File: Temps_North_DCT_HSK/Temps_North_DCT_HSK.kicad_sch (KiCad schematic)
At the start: 4 parts, among them J1 North_Temps_1, J2 North_Temps_2, J3 Internal_Temps_DCT_HSK_Box_1, J4 Internal_Temps_DCT_HSK_Box_2

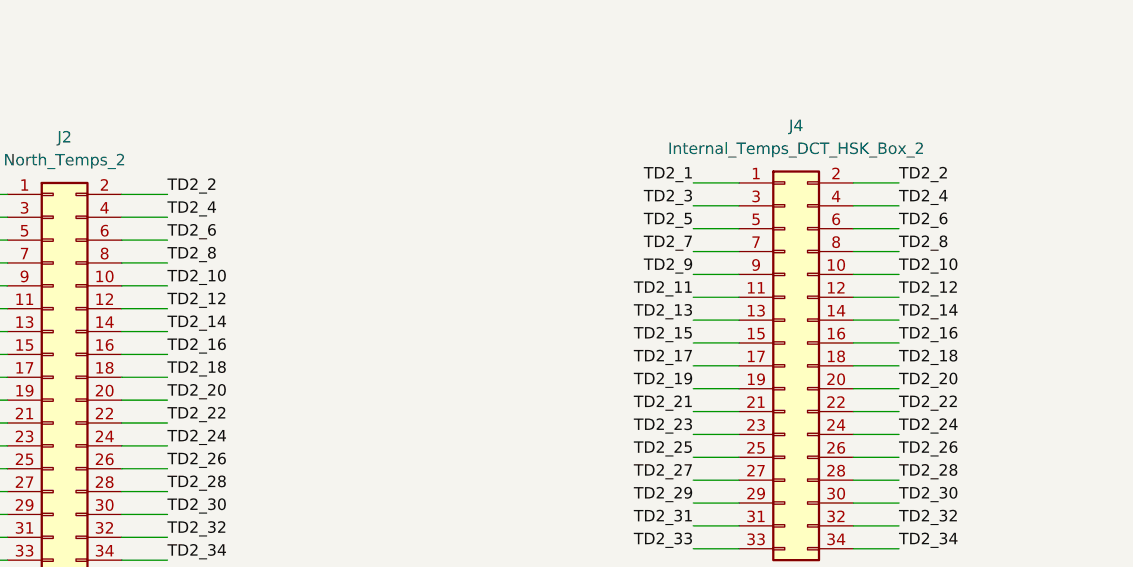
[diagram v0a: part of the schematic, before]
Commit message: Corrected pinout for from NTB2 to DCT HSK
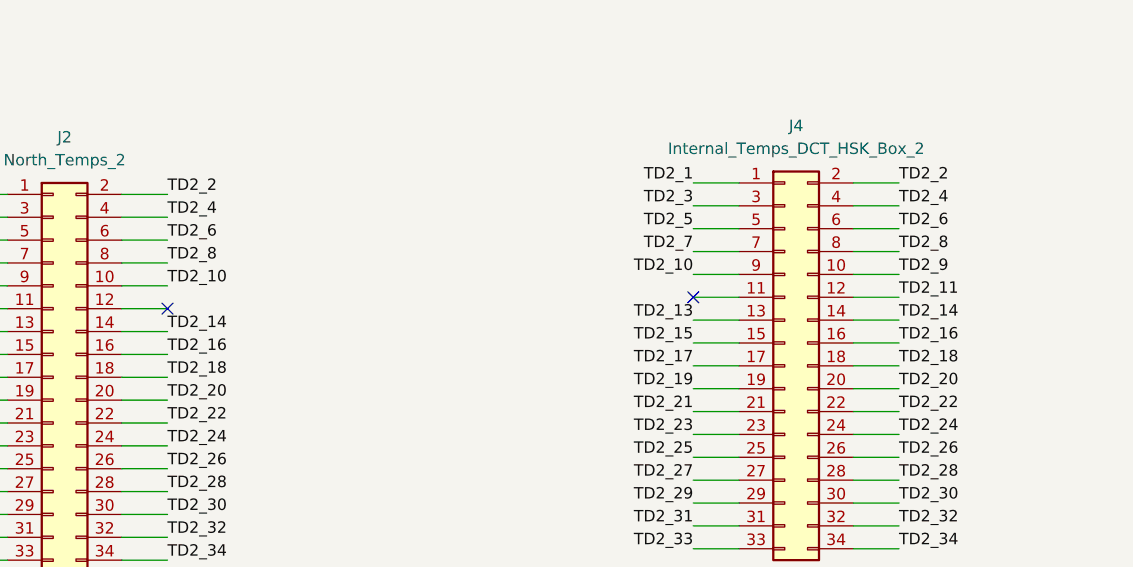
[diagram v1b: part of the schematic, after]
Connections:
- net TD2_10: now also J4.9 (Pin_9); no longer J4.10 (Pin_10)
- net TD2_11: now also J4.12 (Pin_12); no longer J4.11 (Pin_11)
- net TD2_9: now also J4.10 (Pin_10); no longer J4.9 (Pin_9)
- net TD2_12: no longer names the net of J2.12 (Pin_12)
- net TD2_12: no longer J4.12 (Pin_12)
- no-connect marks 0 -> 2
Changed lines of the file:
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@@
     (company "The Ohio State University")
   )
+  (no_connect (at 99.06 130.81))
+  (no_connect (at 157.48 129.54))
   (wire (pts (xy 160.02 78.74) (xy 165.1 78.74))
     (stroke (width 0) (type default) (color 0 0 0 0))
@@
     (effects (font (size 1.27 1.27)) (justify right bottom))
   )
-  (label "TD2_12" (at 180.34 129.54 0)
+  (label "TD2_11" (at 180.34 129.54 0)
     (effects (font (size 1.27 1.27)) (justify left bottom))
   )
@@
     (effects (font (size 1.27 1.27)) (justify right bottom))
   )
-  (label "TD2_11" (at 157.48 129.54 180)
-    (effects (font (size 1.27 1.27)) (justify right bottom))
-  )
   (label "TD1_4" (at 182.88 43.18 0)
     (effects (font (size 1.27 1.27)) (justify left bottom))
@@
     (effects (font (size 1.27 1.27)) (justify right bottom))
   )
-  (label "TD2_9" (at 157.48 127 180)
+  (label "TD2_10" (at 157.48 127 180)
     (effects (font (size 1.27 1.27)) (justify right bottom))
   )
@@
     (effects (font (size 1.27 1.27)) (justify left bottom))
   )
-  (label "TD2_12" (at 99.06 130.81 0)
-    (effects (font (size 1.27 1.27)) (justify left bottom))
-  )
   (label "TD2_2" (at 99.06 118.11 0)
     (effects (font (size 1.27 1.27)) (justify left bottom))
@@
     (effects (font (size 1.27 1.27)) (justify right bottom))
   )
-  (label "TD2_10" (at 180.34 127 0)
-    (effects (font (size 1.27 1.27)) (justify left bottom))
-  )
+  (label "TD2_9" (at 180.34 127 0)
+    (effects (font (size 1.27 1.27)) (justify left bottom))
+  )

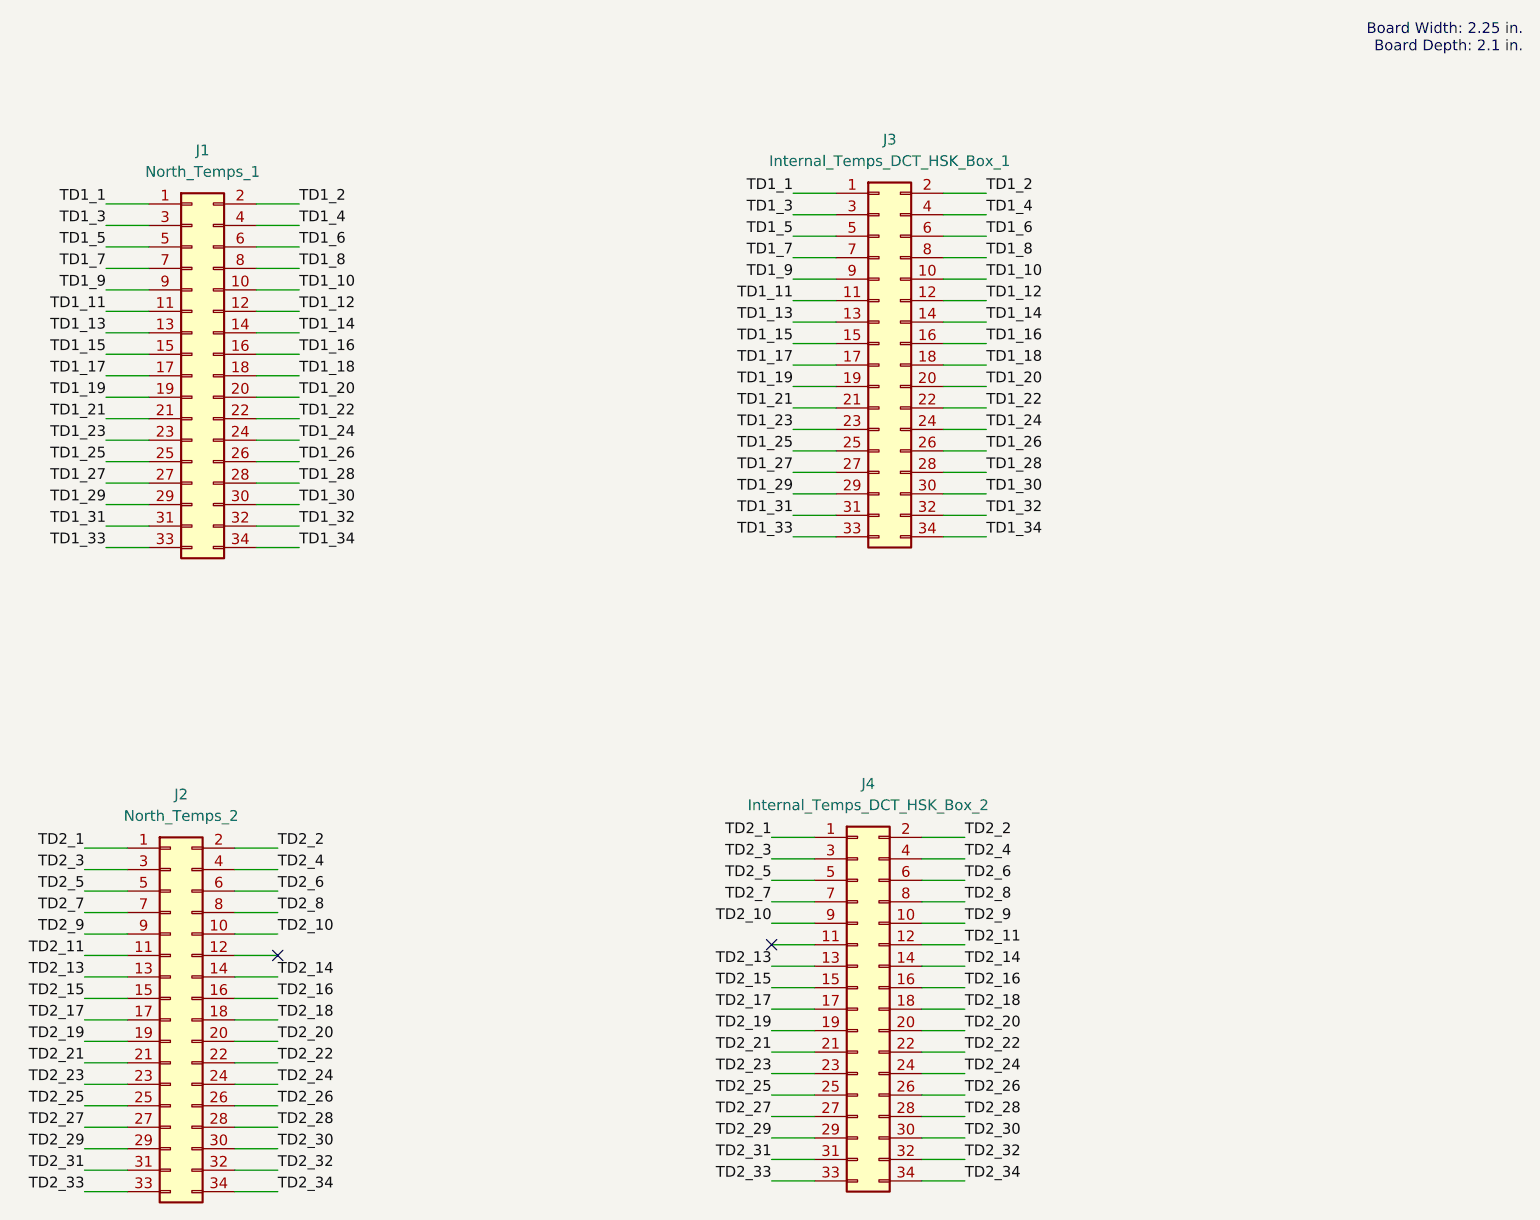
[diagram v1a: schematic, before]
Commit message: Improved temperature PCBs that dont rely on small traces and meet all design rules. Also includes tuned routing for RTD channel.
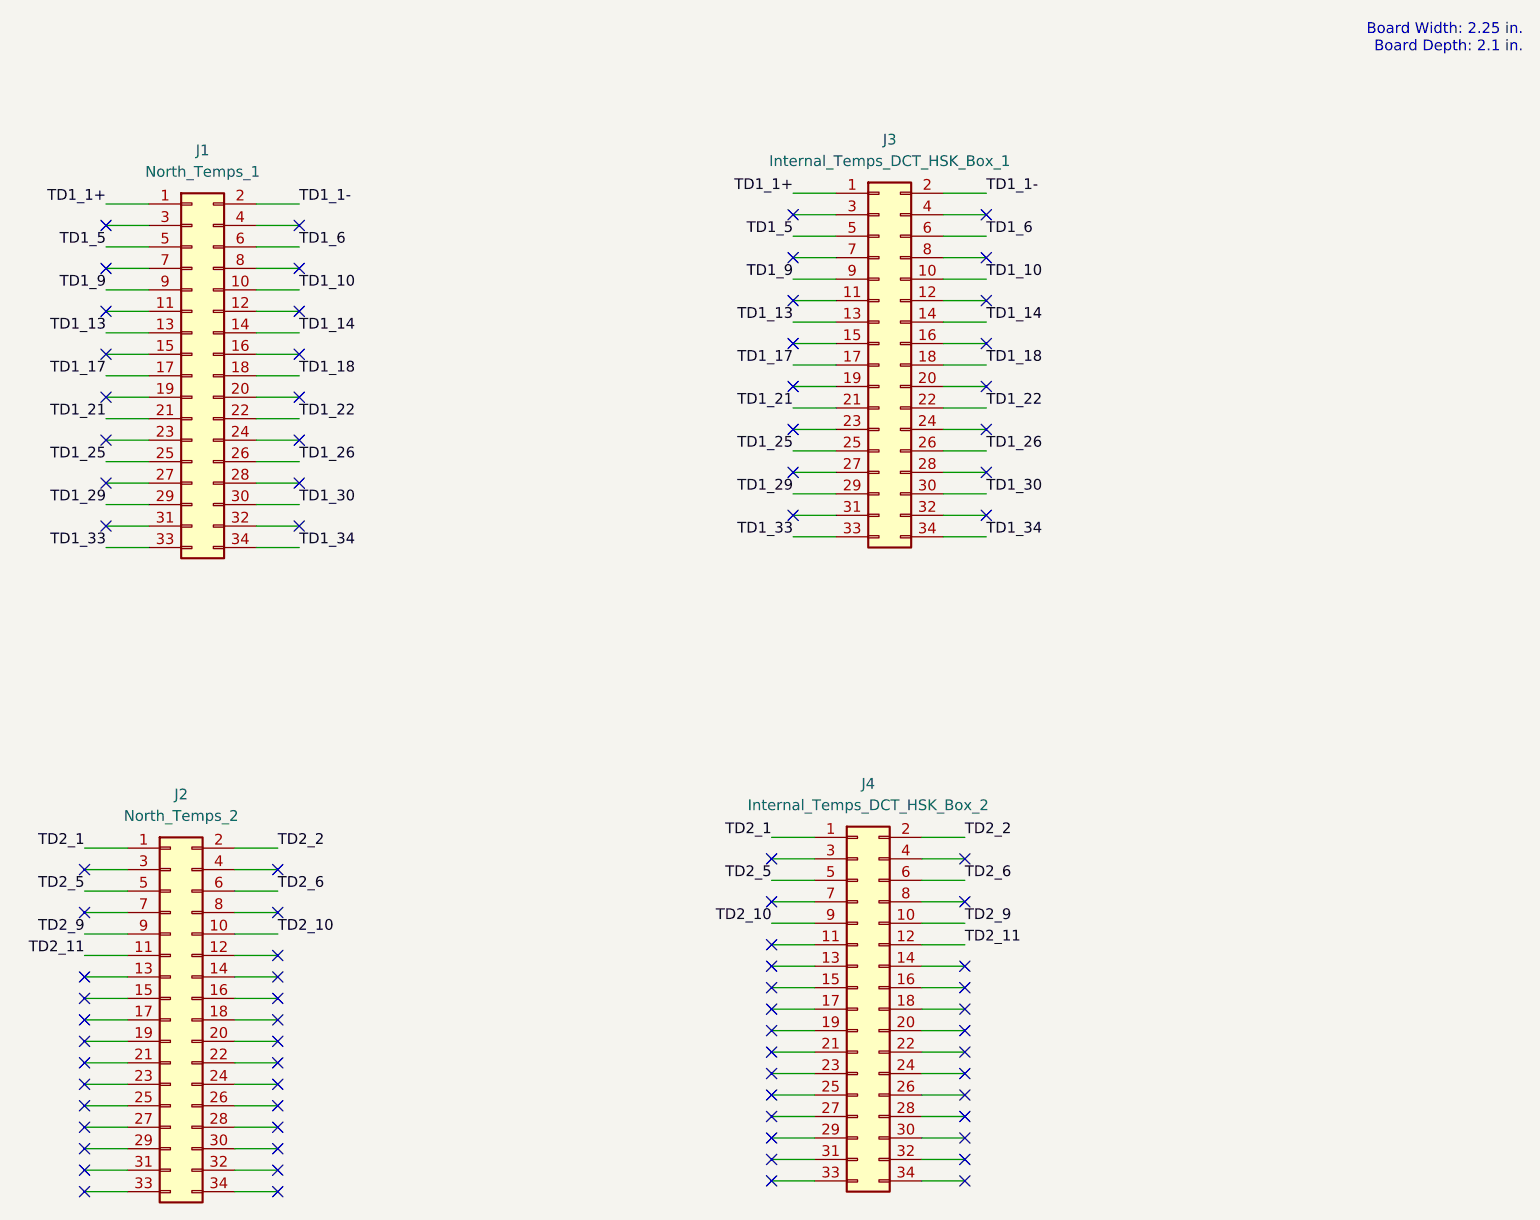
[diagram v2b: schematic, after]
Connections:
- net TD1_1 renamed TD1_1+
- net TD1_11: no longer names the net of J3.11 (Pin_11)
- net TD1_11: no longer J1.11 (Pin_11)
- net TD1_12: no longer names the net of J3.12 (Pin_12)
- net TD1_12: no longer J1.12 (Pin_12)
- net TD1_15: no longer names the net of J3.15 (Pin_15)
- net TD1_15: no longer J1.15 (Pin_15)
- net TD1_16: no longer names the net of J3.16 (Pin_16)
- net TD1_16: no longer J1.16 (Pin_16)
- net TD1_19: no longer names the net of J3.19 (Pin_19)
- net TD1_19: no longer J1.19 (Pin_19)
- net TD1_2 renamed TD1_1-
- net TD1_20: no longer names the net of J3.20 (Pin_20)
- net TD1_20: no longer J1.20 (Pin_20)
- net TD1_23: no longer names the net of J3.23 (Pin_23)
- net TD1_23: no longer J1.23 (Pin_23)
- net TD1_24: no longer names the net of J3.24 (Pin_24)
- net TD1_24: no longer J1.24 (Pin_24)
- net TD1_27: no longer names the net of J3.27 (Pin_27)
- net TD1_27: no longer J1.27 (Pin_27)
- net TD1_28: no longer names the net of J3.28 (Pin_28)
- net TD1_28: no longer J1.28 (Pin_28)
- net TD1_3: no longer names the net of J3.3 (Pin_3)
- net TD1_3: no longer J1.3 (Pin_3)
- net TD1_31: no longer names the net of J3.31 (Pin_31)
- net TD1_31: no longer J1.31 (Pin_31)
- net TD1_32: no longer names the net of J3.32 (Pin_32)
- net TD1_32: no longer J1.32 (Pin_32)
- net TD1_4: no longer names the net of J3.4 (Pin_4)
- net TD1_4: no longer J1.4 (Pin_4)
- net TD1_7: no longer names the net of J3.7 (Pin_7)
- net TD1_7: no longer J1.7 (Pin_7)
- net TD1_8: no longer names the net of J3.8 (Pin_8)
- net TD1_8: no longer J1.8 (Pin_8)
- net TD2_13: no longer names the net of J2.13 (Pin_13)
- net TD2_13: no longer J4.13 (Pin_13)
- net TD2_14: no longer names the net of J2.14 (Pin_14)
- net TD2_14: no longer J4.14 (Pin_14)
- net TD2_15: no longer names the net of J2.15 (Pin_15)
- net TD2_15: no longer J4.15 (Pin_15)
- net TD2_16: no longer names the net of J2.16 (Pin_16)
- net TD2_16: no longer J4.16 (Pin_16)
- net TD2_17: no longer names the net of J2.17 (Pin_17)
- net TD2_17: no longer J4.17 (Pin_17)
- net TD2_18: no longer names the net of J2.18 (Pin_18)
- net TD2_18: no longer J4.18 (Pin_18)
- net TD2_19: no longer names the net of J2.19 (Pin_19)
- net TD2_19: no longer J4.19 (Pin_19)
- net TD2_20: no longer names the net of J2.20 (Pin_20)
- net TD2_20: no longer J4.20 (Pin_20)
- net TD2_21: no longer names the net of J2.21 (Pin_21)
- net TD2_21: no longer J4.21 (Pin_21)
- net TD2_22: no longer names the net of J2.22 (Pin_22)
- net TD2_22: no longer J4.22 (Pin_22)
- net TD2_23: no longer names the net of J2.23 (Pin_23)
- net TD2_23: no longer J4.23 (Pin_23)
- net TD2_24: no longer names the net of J2.24 (Pin_24)
- net TD2_24: no longer J4.24 (Pin_24)
- net TD2_25: no longer names the net of J2.25 (Pin_25)
- net TD2_25: no longer J4.25 (Pin_25)
- net TD2_26: no longer names the net of J2.26 (Pin_26)
- net TD2_26: no longer J4.26 (Pin_26)
- net TD2_27: no longer names the net of J2.27 (Pin_27)
- net TD2_27: no longer J4.27 (Pin_27)
- net TD2_28: no longer names the net of J2.28 (Pin_28)
- net TD2_28: no longer J4.28 (Pin_28)
- net TD2_29: no longer names the net of J2.29 (Pin_29)
- net TD2_29: no longer J4.29 (Pin_29)
- net TD2_3: no longer names the net of J2.3 (Pin_3)
- net TD2_3: no longer J4.3 (Pin_3)
- net TD2_30: no longer names the net of J2.30 (Pin_30)
- net TD2_30: no longer J4.30 (Pin_30)
- net TD2_31: no longer names the net of J2.31 (Pin_31)
- net TD2_31: no longer J4.31 (Pin_31)
- net TD2_32: no longer names the net of J2.32 (Pin_32)
- net TD2_32: no longer J4.32 (Pin_32)
- net TD2_33: no longer names the net of J2.33 (Pin_33)
- net TD2_33: no longer J4.33 (Pin_33)
- net TD2_34: no longer names the net of J2.34 (Pin_34)
- net TD2_34: no longer J4.34 (Pin_34)
- net TD2_4: no longer names the net of J2.4 (Pin_4)
- net TD2_4: no longer J4.4 (Pin_4)
- net TD2_7: no longer names the net of J2.7 (Pin_7)
- net TD2_7: no longer J4.7 (Pin_7)
- net TD2_8: no longer names the net of J2.8 (Pin_8)
- net TD2_8: no longer J4.8 (Pin_8)
- no-connect marks 2 -> 86
